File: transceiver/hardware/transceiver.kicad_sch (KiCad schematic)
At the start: 58 parts, among them J1 Conn_Coaxial, J2 Conn_Coaxial, J3 Conn_01x04, J4 Conn_01x02, J5 Conn_Coaxial, U2 LR2021, U3 STM32G030K8Tx, U4 MAX-M10S, Y1 32.768KHz, Y3 32MHz 10pF

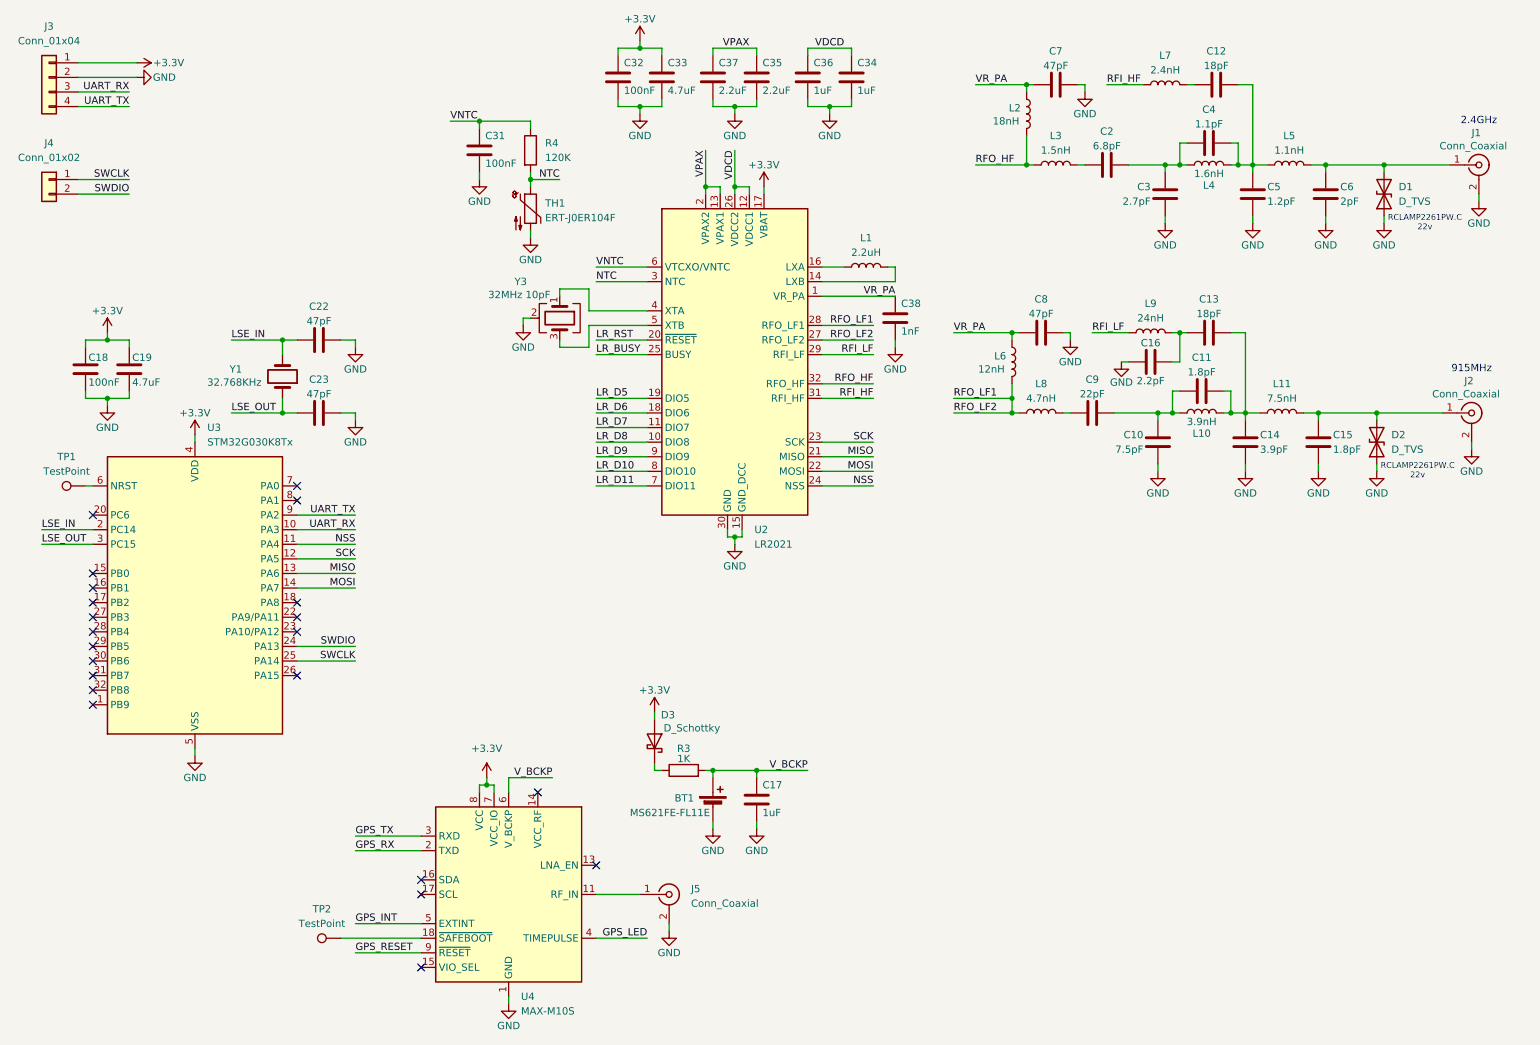
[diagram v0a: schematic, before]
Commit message: finished transceiver pcb
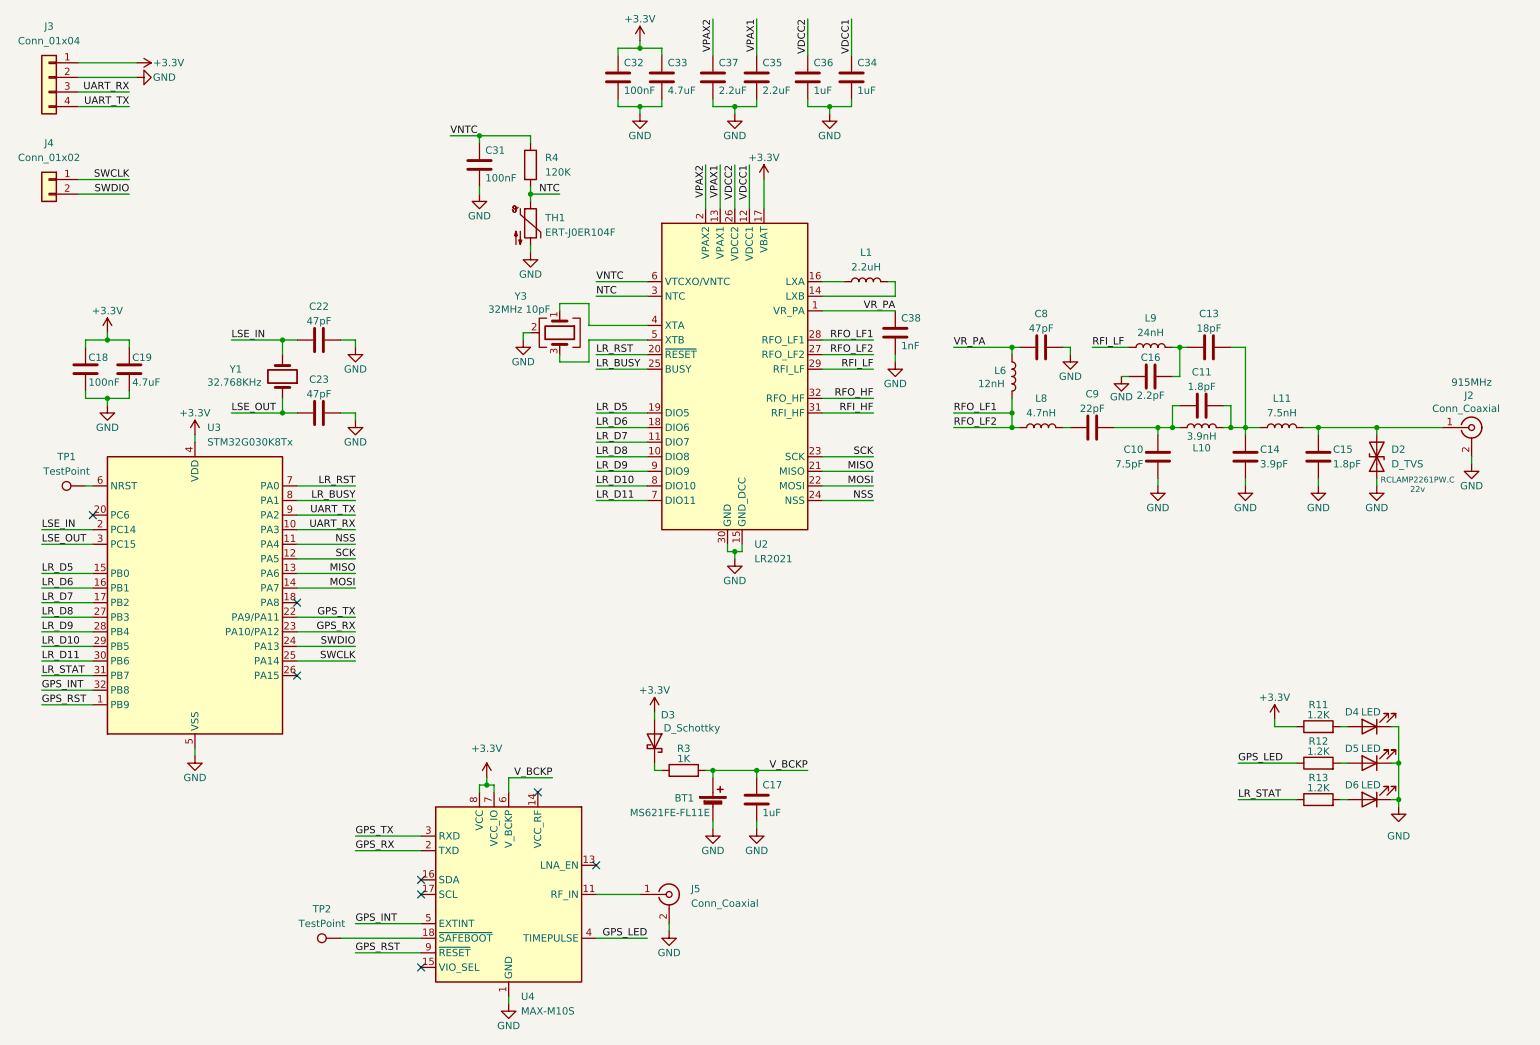
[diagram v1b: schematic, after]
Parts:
- removed C12: 18pF, Capacitor_SMD:C_0402_1005Metric, symbol Device:C
- removed C2: 6.8pF, Capacitor_SMD:C_0402_1005Metric, symbol Device:C
- removed C3: 2.7pF, Capacitor_SMD:C_0402_1005Metric, symbol Device:C
- removed C4: 1.1pF, Capacitor_SMD:C_0402_1005Metric, symbol Device:C
- removed C5: 1.2pF, Capacitor_SMD:C_0402_1005Metric, symbol Device:C
- removed C6: 2pF, Capacitor_SMD:C_0402_1005Metric, symbol Device:C
- removed C7: 47pF, Capacitor_SMD:C_0402_1005Metric, symbol Device:C
- removed D1: D_TVS, Diode_SMD:D_0402_1005Metric, symbol Device:D_TVS
- removed J1: Conn_Coaxial, Connector_Coaxial:U.FL_Molex_MCRF_73412-0110_Vertical, symbol Connector:Conn_Coaxial
- removed L2: 18nH, Inductor_SMD:L_0402_1005Metric, symbol Device:L
- removed L3: 1.5nH, Inductor_SMD:L_0402_1005Metric, symbol Device:L
- removed L4: 1.6nH, Inductor_SMD:L_0402_1005Metric, symbol Device:L
- removed L5: 1.1nH, Inductor_SMD:L_0402_1005Metric, symbol Device:L
- removed L7: 2.4nH, Inductor_SMD:L_0402_1005Metric, symbol Device:L
- added D4, D5, D6: LED, LED_SMD:LED_0603_1608Metric, symbol Device:LED
- added R11, R12, R13: 1.2K, Resistor_SMD:R_0402_1005Metric, symbol Device:R
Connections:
- net GPS_RESET is gone; now on net GPS_RST: U4.9 (~{RESET})
- net +3.3V: now also R11.1
- net GND: now also D4.1 (K), D5.1 (K), D6.1 (K)
- net GPS_INT: now also U3.32 (PB8)
- net GPS_LED: now also R12.1
- net GPS_RX: now also U3.23 (PA10/PA12)
- net GPS_TX: now also U3.22 (PA9/PA11)
- net LR_BUSY: now also U3.8 (PA1)
- net LR_D10: now also U3.29 (PB5)
- net LR_D11: now also U3.30 (PB6)
- net LR_D5: now also U3.15 (PB0)
- net LR_D6: now also U3.16 (PB1)
- net LR_D7: now also U3.17 (PB2)
- net LR_D8: now also U3.27 (PB3)
- net LR_D9: now also U3.28 (PB4)
- net LR_RST: now also U3.7 (PA0)
- net GPS_RST: now reaches U3.1 (PB9)
- net LR_STAT: now reaches U3.31 (PB7)
- net LR_STAT: now also R13.1
- net VDCD renamed VDCC1
- net VDCC1: no longer C36.1, U2.26 (VDCC2)
- net VPAX renamed VPAX1
- net VPAX1: no longer C37.1, U2.2 (VPAX2)
- new net: D6.2 (A), R13.2
- new net: D4.2 (A), R11.2
- new net: D5.2 (A), R12.2
- new net VDCC2: C36.1, U2.26 (VDCC2)
- new net VPAX2: C37.1, U2.2 (VPAX2)
- no-connect marks 22 -> 8
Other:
- note removed: "2.4GHz"
- moved on the sheet: C10, C11, C13, C14, C15, C16, C31, C38, C8, C9, D2, J2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
